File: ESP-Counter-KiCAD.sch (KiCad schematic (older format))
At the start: 43 parts, among them J1 Digital_IP, J2 Motor_Ctrl, J3 LED_Indicator, J4 Orange_Spare, J5 24V_Input, K1 G2RL-1-DC24, K2 G2RL-1-DC24, K3 G2RL-1-DC24, K4 G2RL-1-DC24, K5 G2RL-1-DC24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

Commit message: Footprint association completed
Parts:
- C1, C2, C3, C4: footprint (none) -> Capacitor_SMD:C_0603_1608Metric_Pad1.08x0.95mm_HandSolder
- D1, D2, D3, D4, D5: value 1N4001 -> 1N4007G
- J1, J3, J5: footprint (none) -> Connector_Phoenix_MC_HighVoltage:PhoenixContact_MCV_1,5_4-G-5.08_1x04_P5.08mm_Vertical
- J2: footprint (none) -> Connector_Phoenix_MC_HighVoltage:PhoenixContact_MCV_1,5_6-G-5.08_1x06_P5.08mm_Vertical
- J4: footprint (none) -> Connector_Phoenix_MC_HighVoltage:PhoenixContact_MCV_1,5_5-G-5.08_1x05_P5.08mm_Vertical
- R1, R10, R11, R12, R13, R14, R2, R3, R4, R5, R6, R7, R8, R9: footprint (none) -> Resistor_SMD:R_0805_2012Metric_Pad1.20x1.40mm_HandSolder
- U1: value ESP_12E_J2 -> ESP_12E_J1; footprint (none) -> Connector_PinHeader_2.54mm:PinHeader_1x15_P2.54mm_Vertical
- U10, U3, U4, U5, U7, U8, U9: footprint (none) -> Optocoupler:DIP762W60P254L460H455Q4N
- U2: value ESP_12E_J1 -> ESP_12E_J2; footprint (none) -> Connector_PinHeader_2.54mm:PinHeader_1x15_P2.54mm_Vertical
- U6: footprint (none) -> ULN2801a:DIP850W46P254L2324H393Q18N

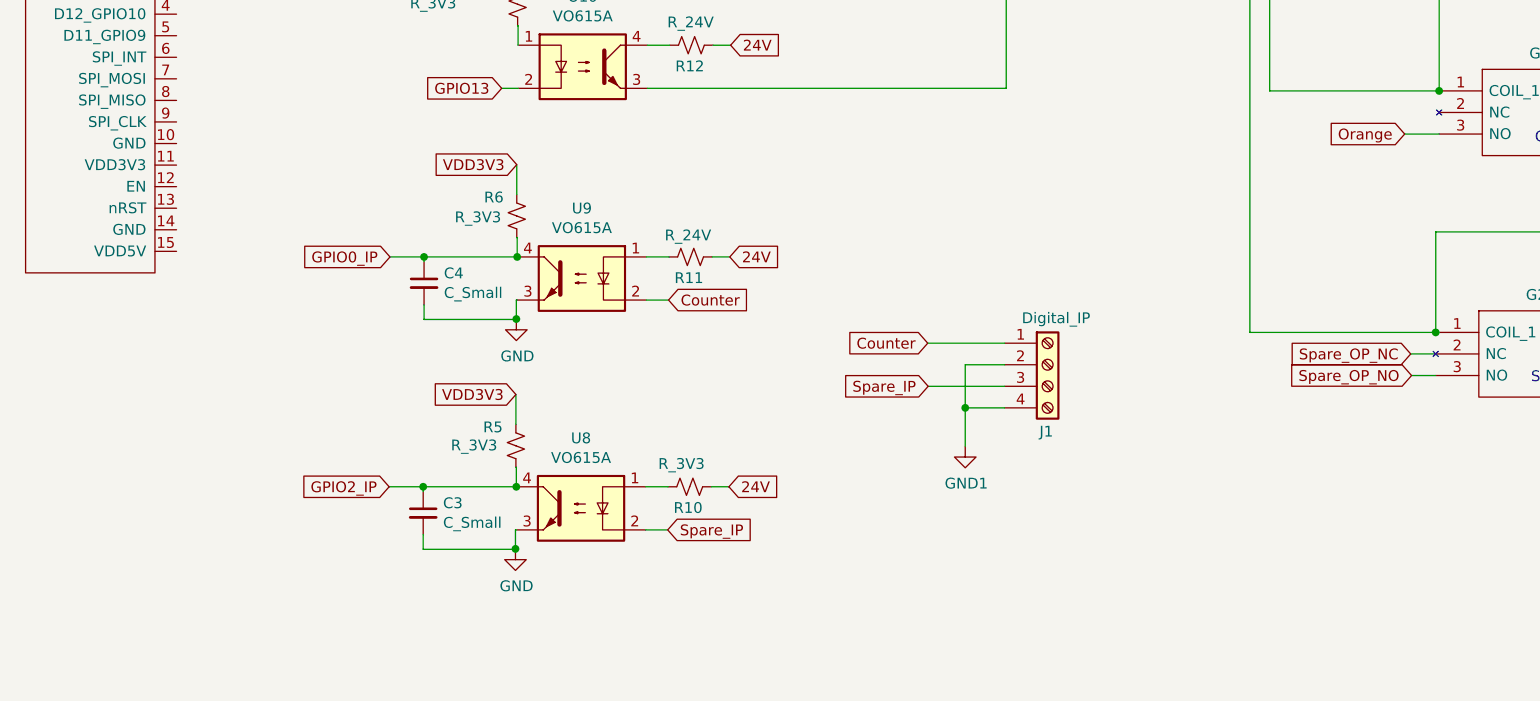
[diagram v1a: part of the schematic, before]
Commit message: DCDC converter symbol added
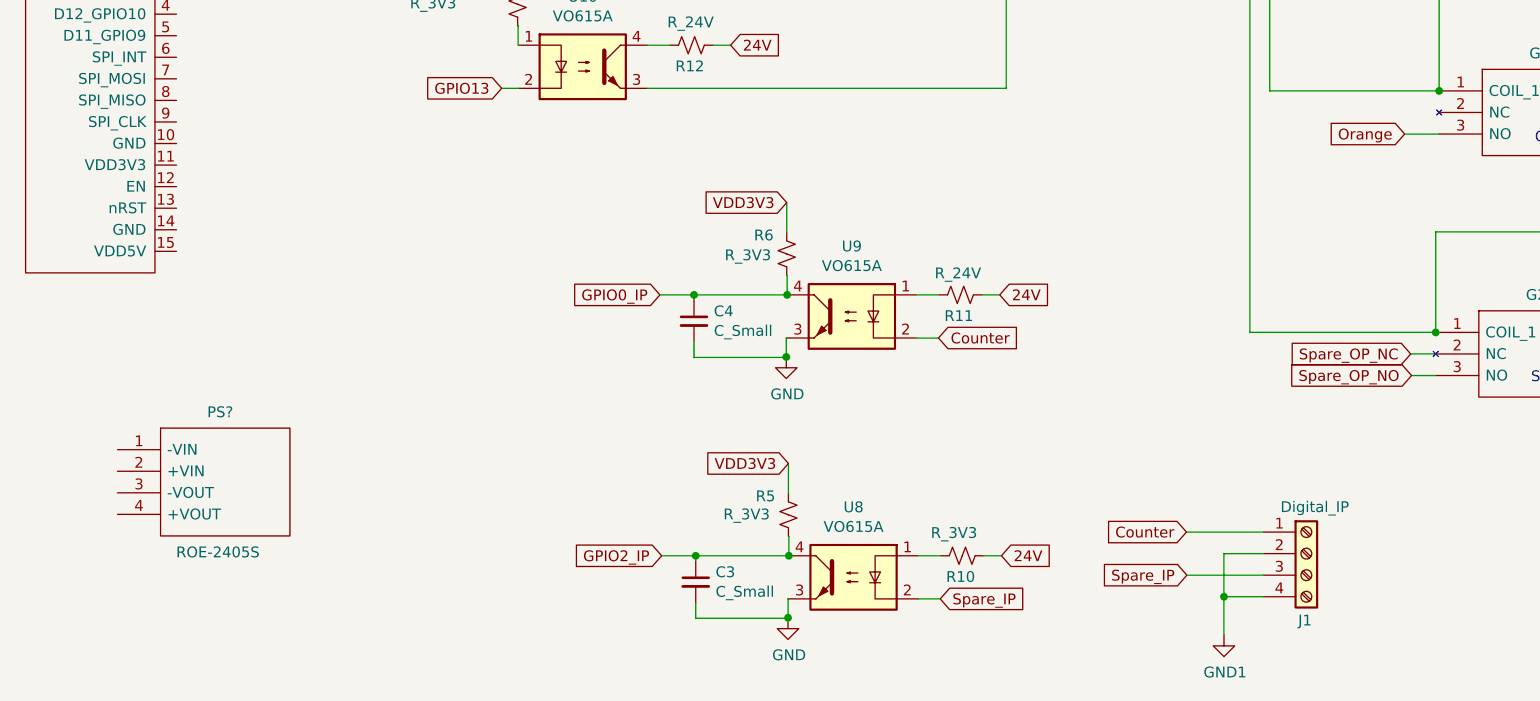
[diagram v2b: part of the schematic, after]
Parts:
- added PS?: ROE-2405S, ROE1205S, symbol ROE-2405S:ROE-2405S
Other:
- moved on the sheet: C3, C4, J1, R10, R11, R5, R6, U8, U9

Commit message: Relays for LED & spare removed, driving LED using ULN
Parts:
- removed D1, D2, D4: 1N4007G, Diode_THT:D_DO-41_SOD81_P10.16mm_Horizontal, symbol Diode:1N4001
- removed J4: Orange_Spare, Connector_Phoenix_MC_HighVoltage:PhoenixContact_MCV_1,5_5-G-5.08_1x05_P5.08mm_Vertical, symbol Connector:Screw_Terminal_01x05
- removed K1, K3, K4: G2RL-1-DC24, SamacSys_Parts:G2RL14, symbol SamacSys_Parts:G2RL-1-DC24
- J3: symbol Connector:Screw_Terminal_01x04 -> Connector:Screw_Terminal_01x06
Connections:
- net labels removed: Spare_OP_COM, Spare_OP_NC, Spare_OP_NO
- wire segments 182 -> 152
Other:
- note removed: "Orange LED"
- note removed: "Red/Green LED"
- note removed: "Spare O/P"
- moved on the sheet: J5, PS?

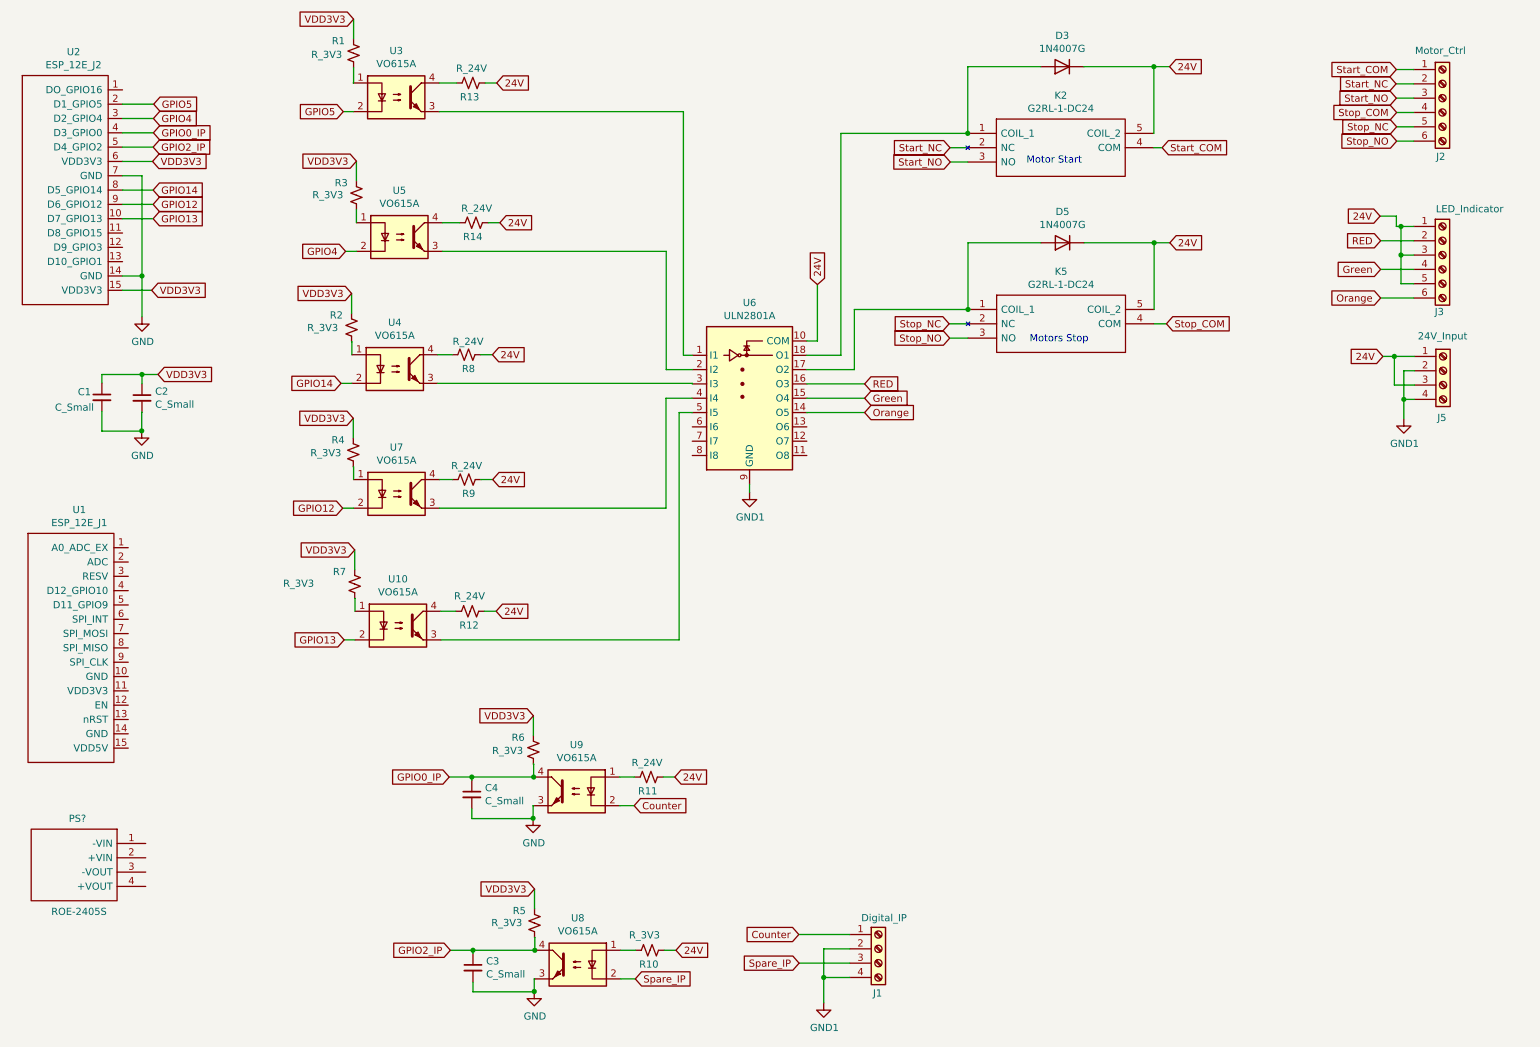
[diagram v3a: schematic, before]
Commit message: Pullup resisitors values updated
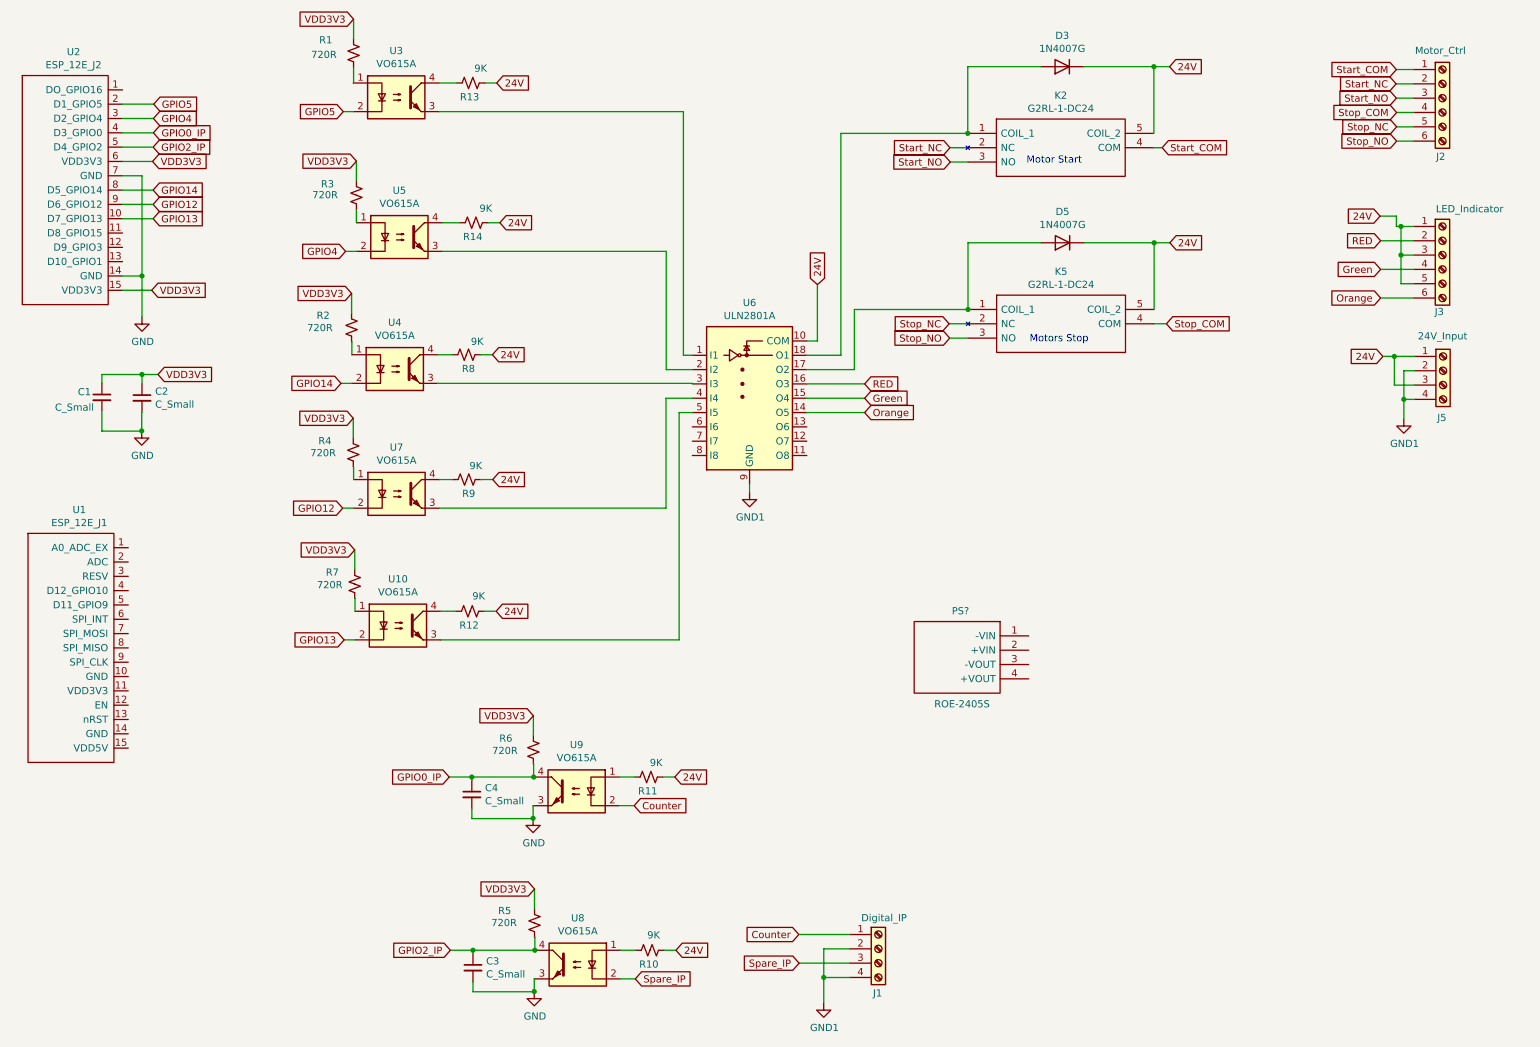
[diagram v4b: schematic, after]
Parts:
- R1, R2, R3, R4, R5, R6, R7: value R_3V3 -> 720R
- R10: value R_3V3 -> 9K
- R11, R12, R13, R14, R8, R9: value R_24V -> 9K
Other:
- moved on the sheet: PS?
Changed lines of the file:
@@
 U 1 1 601B8D73
 P 3074 894
-F 0 "R1" H 2922 980 50  0000 L CNN
-F 1 "R_3V3" H 2778 884 50  0000 L CNN
+F 0 "R1" H 2834 986 50  0000 L CNN
+F 1 "720R" H 2778 884 50  0000 L CNN
 F 2 "Resistor_SMD:R_0805_2012Metric_Pad1.20x1.40mm_HandSolder" H 3074 894 50  0001 C CNN
 F 3 "~" H 3074 894 50  0001 C CNN
@@
 U 1 1 601BD278
 P 3094 1886
-F 0 "R3" H 2942 1972 50  0000 L CNN
-F 1 "R_3V3" H 2786 1888 50  0000 L CNN
+F 0 "R3" H 2846 1964 50  0000 L CNN
+F 1 "720R" H 2786 1888 50  0000 L CNN
 F 2 "Resistor_SMD:R_0805_2012Metric_Pad1.20x1.40mm_HandSolder" H 3094 1886 50  0001 C CNN
 F 3 "~" H 3094 1886 50  0001 C CNN
@@
 U 1 1 601BE4A1
 P 3060 2810
-F 0 "R2" H 2908 2896 50  0000 L CNN
-F 1 "R_3V3" H 2750 2808 50  0000 L CNN
+F 0 "R2" H 2816 2894 50  0000 L CNN
+F 1 "720R" H 2750 2808 50  0000 L CNN
 F 2 "Resistor_SMD:R_0805_2012Metric_Pad1.20x1.40mm_HandSolder" H 3060 2810 50  0001 C CNN
 F 3 "~" H 3060 2810 50  0001 C CNN
@@
 U 1 1 601D6594
 P 3072 3682
-F 0 "R4" H 2920 3768 50  0000 L CNN
-F 1 "R_3V3" H 2772 3678 50  0000 L CNN
+F 0 "R4" H 2828 3762 50  0000 L CNN
+F 1 "720R" H 2772 3678 50  0000 L CNN
 F 2 "Resistor_SMD:R_0805_2012Metric_Pad1.20x1.40mm_HandSolder" H 3072 3682 50  0001 C CNN
 F 3 "~" H 3072 3682 50  0001 C CNN
@@
 U 1 1 601DF2A6
 P 3082 4602
-F 0 "R7" H 2930 4688 50  0000 L CNN
-F 1 "R_3V3" H 2582 4606 50  0000 L CNN
+F 0 "R7" H 2880 4684 50  0000 L CNN
+F 1 "720R" H 2818 4596 50  0000 L CNN
 F 2 "Resistor_SMD:R_0805_2012Metric_Pad1.20x1.40mm_HandSolder" H 3082 4602 50  0001 C CNN
 F 3 "~" H 3082 4602 50  0001 C CNN
@@
 P 3892 1102
 F 0 "R13" V 3794 1042 50  0000 L CNN
-F 1 "R_24V" V 3994 988 50  0000 L CNN
+F 1 "9K" V 3994 988 50  0000 L CNN
 F 2 "Resistor_SMD:R_0805_2012Metric_Pad1.20x1.40mm_HandSolder" H 3892 1102 50  0001 C CNN
 F 3 "~" H 3892 1102 50  0001 C CNN
@@
 P 3914 2078
 F 0 "R14" V 3816 2018 50  0000 L CNN
-F 1 "R_24V" V 4014 1950 50  0000 L CNN
+F 1 "9K" V 4014 1950 50  0000 L CNN
 F 2 "Resistor_SMD:R_0805_2012Metric_Pad1.20x1.40mm_HandSolder" H 3914 2078 50  0001 C CNN
 F 3 "~" H 3914 2078 50  0001 C CNN
@@
 P 3862 3000
 F 0 "R8" V 3764 2940 50  0000 L CNN
-F 1 "R_24V" V 3954 2880 50  0000 L CNN
+F 1 "9K" V 3954 2880 50  0000 L CNN
 F 2 "Resistor_SMD:R_0805_2012Metric_Pad1.20x1.40mm_HandSolder" H 3862 3000 50  0001 C CNN
 F 3 "~" H 3862 3000 50  0001 C CNN
@@
 P 3864 3872
 F 0 "R9" V 3766 3812 50  0000 L CNN
-F 1 "R_24V" V 3960 3764 50  0000 L CNN
+F 1 "9K" V 3960 3764 50  0000 L CNN
 F 2 "Resistor_SMD:R_0805_2012Metric_Pad1.20x1.40mm_HandSolder" H 3864 3872 50  0001 C CNN
 F 3 "~" H 3864 3872 50  0001 C CNN
@@
 P 3888 4792
 F 0 "R12" V 3790 4732 50  0000 L CNN
-F 1 "R_24V" V 3994 4688 50  0000 L CNN
+F 1 "9K" V 3994 4688 50  0000 L CNN
 F 2 "Resistor_SMD:R_0805_2012Metric_Pad1.20x1.40mm_HandSolder" H 3888 4792 50  0001 C CNN
 F 3 "~" H 3888 4792 50  0001 C CNN
@@
 P 5136 5950
 F 0 "R11" V 5038 5890 50  0000 L CNN
-F 1 "R_24V" V 5236 5854 50  0000 L CNN
+F 1 "9K" V 5236 5854 50  0000 L CNN
 F 2 "Resistor_SMD:R_0805_2012Metric_Pad1.20x1.40mm_HandSolder" H 5136 5950 50  0001 C CNN
 F 3 "~" H 5136 5950 50  0001 C CNN
@@
 U 1 1 603034FD
 P 4330 5760
-F 0 "R6" H 4178 5846 50  0000 L CNN
-F 1 "R_3V3" H 4042 5754 50  0000 L CNN
+F 0 "R6" H 4092 5840 50  0000 L CNN
+F 1 "720R" H 4042 5754 50  0000 L CNN
 F 2 "Resistor_SMD:R_0805_2012Metric_Pad1.20x1.40mm_HandSolder" H 4330 5760 50  0001 C CNN
 F 3 "~" H 4330 5760 50  0001 C CNN
@@
 P 5144 7160
 F 0 "R10" V 5046 7100 50  0000 L CNN
-F 1 "R_3V3" V 5250 7090 50  0000 L CNN
+F 1 "9K" V 5250 7090 50  0000 L CNN
 F 2 "Resistor_SMD:R_0805_2012Metric_Pad1.20x1.40mm_HandSolder" H 5144 7160 50  0001 C CNN
 F 3 "~" H 5144 7160 50  0001 C CNN
@@
 U 1 1 6033C912
 P 4338 6970
-F 0 "R5" H 4186 7056 50  0000 L CNN
-F 1 "R_3V3" H 4036 6972 50  0000 L CNN
+F 0 "R5" H 4084 7056 50  0000 L CNN
+F 1 "720R" H 4036 6972 50  0000 L CNN
 F 2 "Resistor_SMD:R_0805_2012Metric_Pad1.20x1.40mm_HandSolder" H 4338 6970 50  0001 C CNN
 F 3 "~" H 4338 6970 50  0001 C CNN
@@
 L ROE-2405S:ROE-2405S PS?
 U 1 1 601CB8A2
-P 1622 6414
-F 0 "PS?" H 2038 6588 50  0000 L CNN
-F 1 "ROE-2405S" H 1894 5938 50  0000 L CNN
-F 2 "ROE1205S" H 2472 6514 50  0001 L CNN
-F 3 "https://recom-power.com/pdf/Econoline/ROE.pdf" H 2472 6414 50  0001 L CNN
-F 4 "Recom Through Hole 1W Isolated DC-DC Converter, I/O isolation 1kV dc, Vout 5V dc" H 2472 6314 50  0001 L CNN "Description"
-F 5 "10.5" H 2472 6214 50  0001 L CNN "Height"
-F 6 "RECOM Power" H 2472 6114 50  0001 L CNN "Manufacturer_Name"
-F 7 "ROE-2405S" H 2472 6014 50  0001 L CNN "Manufacturer_Part_Number"
-F 8 "919-ROE-2405S" H 2472 5914 50  0001 L CNN "Mouser Part Number"
-F 9 "https://www.mouser.co.uk/ProductDetail/RECOM-Power/ROE-2405S/?qs=wlO1EFRhkBD1PQdCwpEhnw%3D%3D" H 2472 5814 50  0001 L CNN "Mouser Price/Stock"
-F 10 "ROE-2405S" H 2472 5714 50  0001 L CNN "Arrow Part Number"
-F 11 "https://www.arrow.com/en/products/roe-2405s/recom-power" H 2472 5614 50  0001 L CNN "Arrow Price/Stock"
-	1    1622 6414
+P 7790 4964
+F 0 "PS?" H 8206 5138 50  0000 L CNN
+F 1 "ROE-2405S" H 8062 4488 50  0000 L CNN
+F 2 "ROE1205S" H 8640 5064 50  0001 L CNN
+F 3 "https://recom-power.com/pdf/Econoline/ROE.pdf" H 8640 4964 50  0001 L CNN
+F 4 "Recom Through Hole 1W Isolated DC-DC Converter, I/O isolation 1kV dc, Vout 5V dc" H 8640 4864 50  0001 L CNN "Description"
+F 5 "10.5" H 8640 4764 50  0001 L CNN "Height"
+F 6 "RECOM Power" H 8640 4664 50  0001 L CNN "Manufacturer_Name"
+F 7 "ROE-2405S" H 8640 4564 50  0001 L CNN "Manufacturer_Part_Number"
+F 8 "919-ROE-2405S" H 8640 4464 50  0001 L CNN "Mouser Part Number"
+F 9 "https://www.mouser.co.uk/ProductDetail/RECOM-Power/ROE-2405S/?qs=wlO1EFRhkBD1PQdCwpEhnw%3D%3D" H 8640 4364 50  0001 L CNN "Mouser Price/Stock"
+F 10 "ROE-2405S" H 8640 4264 50  0001 L CNN "Arrow Part Number"
+F 11 "https://www.arrow.com/en/products/roe-2405s/recom-power" H 8640 4164 50  0001 L CNN "Arrow Price/Stock"
+	1    7790 4964
 	-1   0    0    -1
 $EndComp
